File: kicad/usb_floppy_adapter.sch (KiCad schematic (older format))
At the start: 24 parts, among them J1 Conn_02x17_Odd_Even, J2 MICRO_USB_B, J3 Conn_01x02, J4 Conn_01x04, J5 GS2, J6 GS2, J7 GS3, U1 LM1117-3.3, U2 STM32F103C8Tx, U3 USBLC6-2SC6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

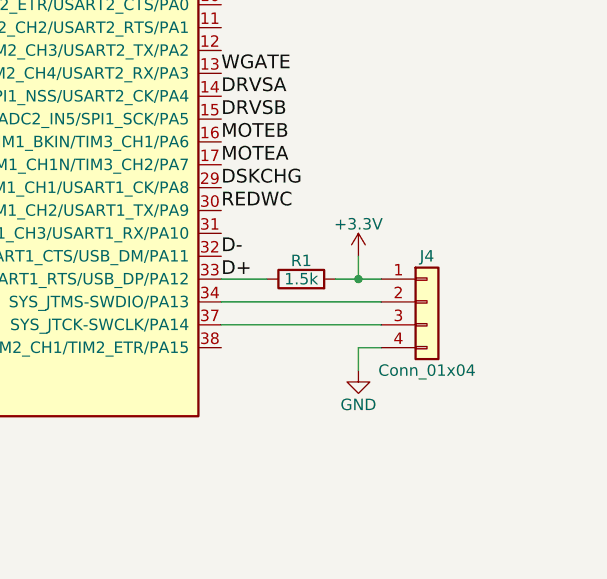
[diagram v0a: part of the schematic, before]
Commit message: add termination resistors
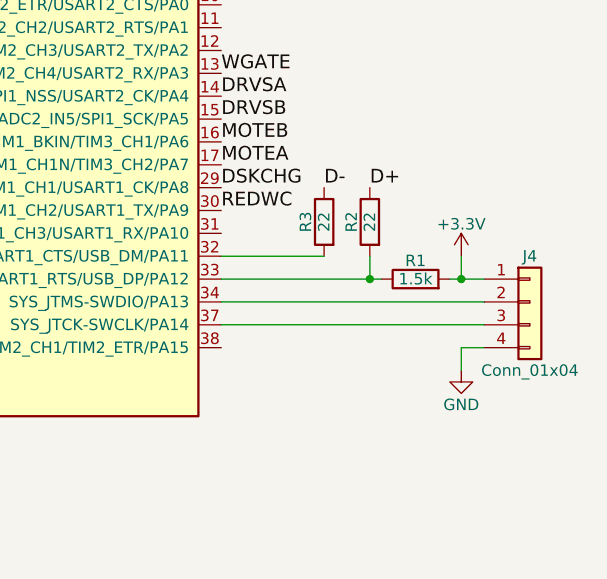
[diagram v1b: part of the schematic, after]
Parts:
- added R2, R3: 22, Resistors_SMD:R_0603, symbol R
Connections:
- net D+: now also R2.1; no longer R1.1, U2.33 (CAN_TX/TIM1_ETR/USART1_RTS/USB_DP/PA12)
- net D-: now also R3.1; no longer U2.32 (ADC1_EXTI11/ADC2_EXTI11/CAN_RX/TIM1_CH4/USART1_CTS/USB_DM/PA11)
- new net: R3.2, U2.32 (ADC1_EXTI11/ADC2_EXTI11/CAN_RX/TIM1_CH4/USART1_CTS/USB_DM/PA11)
- new net: R1.1, R2.2, U2.33 (CAN_TX/TIM1_ETR/USART1_RTS/USB_DP/PA12)
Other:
- moved on the sheet: J4, R1

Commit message: Preparations for first prototype run
- Tie BOOT0 to GND to ensure proper boot-up
- Mark all unused MCU pins in the schematic as N/C
- Double the width of the most important 5V and 12V traces
- Move some traces further away from pads
- Optimize parameters of Copper Fills
- Add meta data and revision number (revision 0)
- Include URL and revision number in silk screen text
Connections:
- net GND: now also U2.44 (BOOT0)
- no-connect marks 1 -> 18
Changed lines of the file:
@@
 encoding utf-8
 Sheet 1 1
-Title ""
-Date ""
-Rev ""
-Comp ""
+Title "USB Floppy Adapter"
+Date "2018-03-03"
+Rev "0"
+Comp "Benedikt Freisen"
 Comment1 ""
 Comment2 ""
 Comment3 ""
-Comment4 ""
+Comment4 "STM32-based USB to Floppy-Disk Drive (FDD) Adapter"
 $EndDescr
 $Comp
@@
 Wire Wire Line
 	10600 4600 10750 4600
+NoConn ~ 9600 3500
+NoConn ~ 9600 3600
+NoConn ~ 9600 4400
+NoConn ~ 9600 4900
+NoConn ~ 3800 2100
+NoConn ~ 3800 2500
+NoConn ~ 3800 3000
+NoConn ~ 3800 3100
+NoConn ~ 3800 3200
+NoConn ~ 3800 3600
+NoConn ~ 3800 3700
+NoConn ~ 3800 3800
+NoConn ~ 3800 3900
+NoConn ~ 3800 4000
+NoConn ~ 3800 4100
+NoConn ~ 3800 4200
+NoConn ~ 3800 4300
+$Comp
+L GND #PWR?
+U 1 1 5A9ADE2C
+P 3600 2300
+F 0 "#PWR?" H 3600 2050 50  0001 C CNN
+F 1 "GND" H 3600 2150 50  0000 C CNN
+F 2 "" H 3600 2300 50  0001 C CNN
+F 3 "" H 3600 2300 50  0001 C CNN
+	1    3600 2300
+	1    0    0    -1
+$EndComp
+Wire Wire Line
+	3600 2300 3800 2300
 $EndSCHEMATC
